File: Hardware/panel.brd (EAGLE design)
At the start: 79 x 43 mm, 18 parts, among them X1 B16B-PHDSS, X2 52746-20

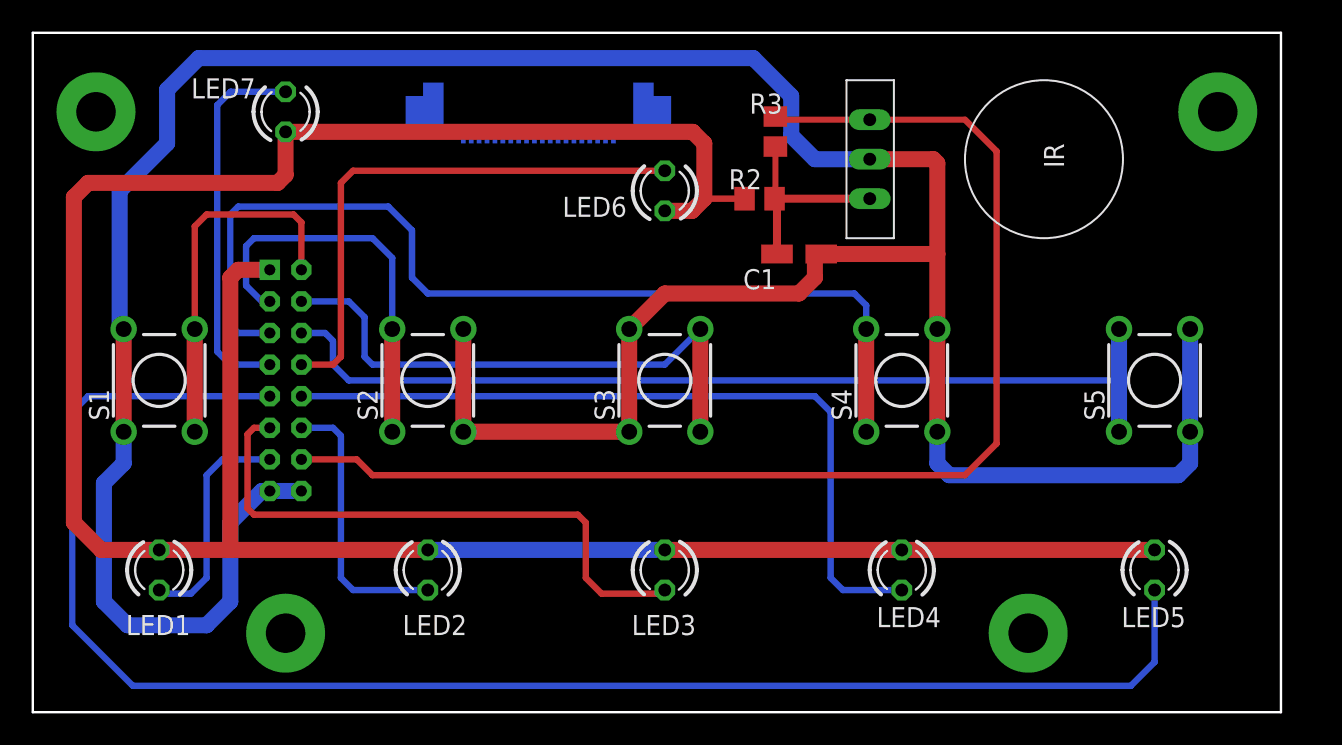
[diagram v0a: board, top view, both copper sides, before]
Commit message: разъем под шлейф,вывод для штатного питания прибора. Сделал цепи комутации кнопок на транзисторе.
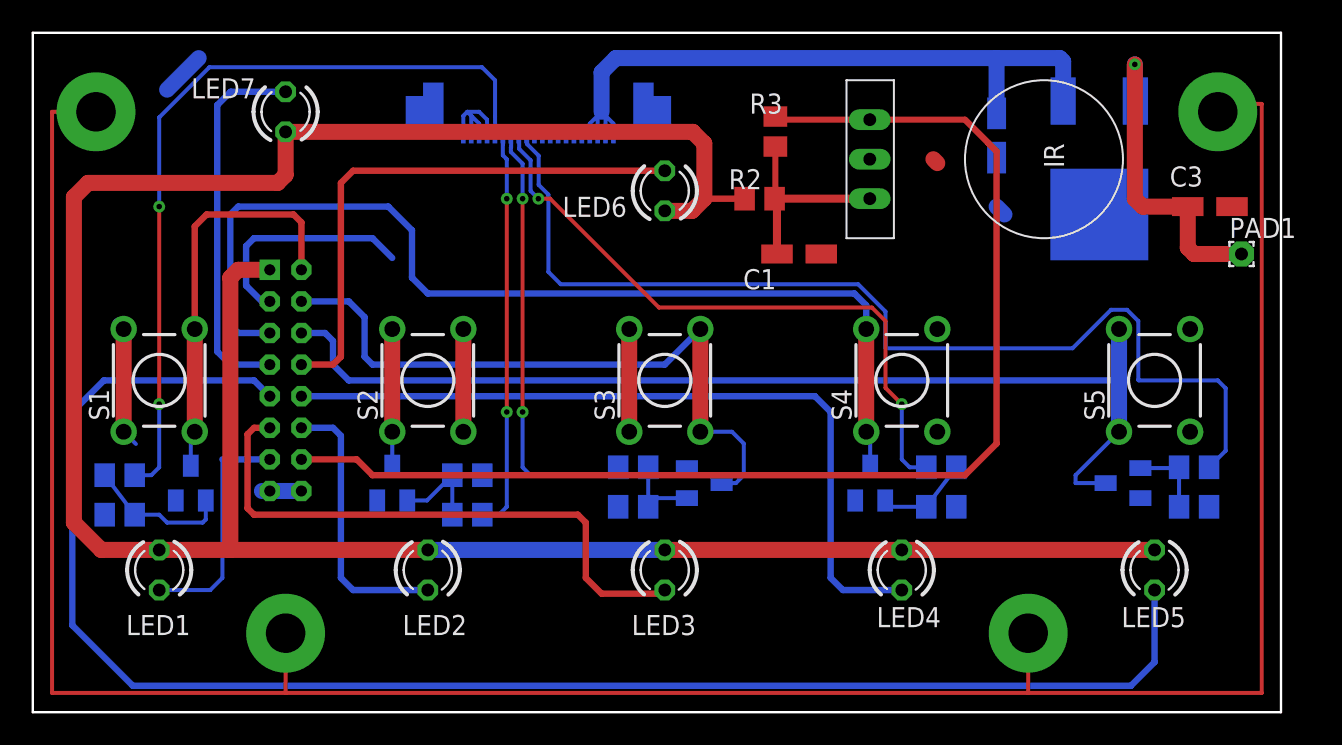
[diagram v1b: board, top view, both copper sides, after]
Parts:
- added C2: 0.33uF, rcl:CT3216
- added C3: 0.1uF, rcl:CT3216
- added PAD1: (no value), wirepad:1,6/0,8
- added Q1, Q2, Q3, Q4, Q5: BC817-40LT1SMD, transistor-npn:SOT23-BEC
- added R1, R10, R11, R12, R4, R5, R6, R7, R8, R9: 4.7k, rcl:R0805
- added U1: MC7805CDT, _hhn_78xx_79xx_NCV78xx_d2pak_dpak:DPAK-3
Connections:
- new net +24V: C2.+, U1.1, X2.17, X2.18, X2.19, X2.20
- new net FF_SIG: R12.2, X2.9
- new net FN_SIG: R10.2, X2.8
- new net LASER_SIG: R8.2, X2.7
- new net N$1: Q1.B, R1.2, R4.1
- new net N$3: S3.1, S3.3
- new net N$4: Q2.B, R5.2, R6.1
- new net N$5: Q3.B, R7.2, R8.1
- new net N$6: Q4.B, R10.1, R9.2
- new net N$7: Q5.B, R11.2, R12.1
- new net PRW_SIG: R4.2, X2.5
- new net SET_SIG: R6.2, X2.6
- new net VOUT_SB: C3.+, PAD1.1, U1.3
- net FFSW: now also Q5.C
- net FNSW: now also Q4.C
- net GND: now also C2.-, C3.-, Q1.E, Q2.E, Q3.E, Q4.E, Q5.E, R1.1, R11.1, R5.1, R7.1, R9.1, U1.4, X2.1, X2.2, X2.3, X2.4; no longer S3.1, S3.3
- net LASERSW: now also Q3.C
- net PWR_SW: now also Q1.C
- net SETSW: now also Q2.C
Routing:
- net FF_SIG: track 0.00 -> 66.0 mm
- net PRW_SIG: track 0.00 -> 50.4 mm, vias 0 -> 2
- net +24V: track 0.00 -> 44.7 mm
- net FN_SIG: track 0.00 -> 40.5 mm, vias 0 -> 2
- net LASER_SIG: track 0.00 -> 27.7 mm, vias 0 -> 2
- net SET_SIG: track 0.00 -> 25.5 mm, vias 0 -> 2
- net VOUT_SB: track 0.00 -> 20.6 mm, vias 0 -> 1
- net N$1: track 0.00 -> 9.13 mm, vias 1 -> 0
- net LASERSW: track 35.8 -> 42.5 mm
- net N$3: track 0.00 -> 6.50 mm, vias 1 -> 0
- net FFSW: track 60.4 -> 66.7 mm
- net N$4: track 0.00 -> 6.01 mm, vias 1 -> 0
- net N$6: track 0.00 -> 5.91 mm
- net N$5: track 0.00 -> 5.18 mm, vias 1 -> 0
- net N$7: track 0.00 -> 4.97 mm
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- added copper zone on layer 1, net GND
- added copper zone on layer 16, net GND

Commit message: переподключил индикаторы через транзисторы. это надо испытать
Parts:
- added Q10, Q11, Q12, Q6, Q7, Q8, Q9: BC807-16LT1SMD, transistor-pnp:SOT23-BEC
- added Q13, Q14, Q15, Q16, Q17, Q18, Q19: BC817-40LT1SMD, transistor-npn:SOT23-BEC
- added R13, R15, R16, R18, R19, R21, R22, R24, R25, R27, R28, R30, R31, R33, R34, R36, R38, R40, R42, R44, R46: 4.7k, rcl:R0805
- added R14, R17, R20, R23, R26, R29, R32: 2.2k, rcl:R0805
- added R35, R37, R39, R41, R43, R45, R47: 800, rcl:R0805
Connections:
- new net ADJLED_SIG: LED2.A, Q9.C, X2.11
- new net DOWNLED_SIG: LED3.A, Q10.C, X2.12
- new net LVLLED_SIG: LED7.A, Q6.C, X2.16
- new net N$10: LED7.K, R14.2
- new net N$11: Q14.B, R36.1, R37.2
- new net N$12: Q7.B, R15.1, R18.1
- new net N$13: LED6.K, R17.2
- new net N$14: Q8.B, R19.1, R21.1
- new net N$15: LED1.K, R20.2
- new net N$16: Q9.B, R22.1, R24.1
- new net N$17: LED2.K, R23.2
- new net N$18: Q10.B, R25.1, R27.1
- new net N$19: LED3.K, R26.2
- new net N$20: Q11.B, R28.1, R30.1
- new net N$21: LED4.K, R29.2
- new net N$22: Q12.B, R31.1, R33.1
- new net N$23: LED5.K, R32.2
- new net N$24: Q13.B, R34.1, R35.2
- new net N$25: Q14.C, R15.2
- new net N$26: Q15.B, R38.1, R39.2
- new net N$27: Q15.C, R31.2
- new net N$28: Q16.B, R40.1, R41.2
- new net N$29: Q16.C, R28.2
- new net N$30: Q17.B, R42.1, R43.2
- new net N$31: Q17.C, R25.2
- new net N$32: Q18.B, R44.1, R45.2
- new net N$33: Q18.C, R22.2
- new net N$34: Q19.B, R46.1, R47.2
- new net N$35: Q19.C, R19.2
- new net N$8: Q6.B, R13.1, R16.1
- new net N$9: Q13.C, R13.2
- new net PWRLED_SIG: LED1.A, Q8.C, X2.10
- new net UPLED_SIG: LED6.A, Q7.C, X2.15
- new net XLED_SIG: LED4.A, Q11.C, X2.13
- new net YLED_SIG: LED5.A, Q12.C, X2.14
- net +24V: now also Q10.E, Q11.E, Q12.E, Q6.E, Q7.E, Q8.E, Q9.E, R16.2, R18.2, R21.2, R24.2, R27.2, R30.2, R33.2
- net +5V: now also R35.1, R37.1, R39.1, R41.1, R43.1, R45.1, R47.1; no longer LED1.A, LED2.A, LED3.A, LED4.A, LED5.A, LED6.A, LED7.A
- net ADJLED: now also Q18.E, R44.2; no longer LED2.K
- net DOWNLED: now also Q17.E, R42.2; no longer LED3.K
- net GND: now also R14.1, R17.1, R20.1, R23.1, R26.1, R29.1, R32.1
- net LVLED: now also Q13.E, R34.2; no longer LED7.K
- net PWRLED: now also Q19.E, R46.2; no longer LED1.K
- net UPLED: now also Q14.E, R36.2; no longer LED6.K
- net XLED: now also Q16.E, R40.2; no longer LED4.K
- net YLED: now also Q15.E, R38.2; no longer LED5.K
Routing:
- net +5V: track 162.0 -> 28.1 mm
- net UPLED: track 34.5 -> 14.8 mm
- net ADJLED: track 17.5 -> 12.8 mm
- net YLED: track 102.5 -> 98.0 mm
- net XLED: track 49.2 -> 45.5 mm
- net LVLED: track 23.9 -> 20.5 mm
- net PWRLED: track 14.8 -> 11.6 mm

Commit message: сделал разводку управляющих и индикаторных цепей на транзисторах. еще не проверял работоспособность решений.
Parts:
- moved R47 237.1 mm to (10.0, 5.50), flipped to the bottom
- moved R46 233.9 mm to (11.0, 2.00), flipped to the bottom, turned to 90 degrees
- moved Q19 227.2 mm to (8.00, 2.50), flipped to the bottom, turned to 180 degrees
- moved R44 222.2 mm to (29.0, 2.50), flipped to the bottom, turned to 90 degrees
- moved R45 221.9 mm to (32.0, 2.50), flipped to the bottom, turned to 270 degrees
- moved R43 218.2 mm to (45.5, 10.5), flipped to the bottom, turned to 270 degrees
- moved Q18 214.3 mm to (25.5, 2.00), flipped to the bottom, turned to 180 degrees
- moved R42 211.2 mm to (44.0, 2.50), flipped to the bottom, turned to 270 degrees
- moved R41 206.9 mm to (63.0, 8.50), flipped to the bottom, turned to 270 degrees
- moved R40 205.6 mm to (58.0, 7.00), flipped to the bottom, turned to 180 degrees
- moved Q17 203.5 mm to (40.0, 2.50), flipped to the bottom, turned to 180 degrees
- moved R36 198.2 mm to (42.5, 31.5), flipped to the bottom
- moved R37 198.0 mm to (47.0, 31.5), flipped to the bottom
- moved R39 196.0 mm to (74.5, 7.00), flipped to the bottom, turned to 180 degrees
- moved R38 195.8 mm to (74.5, 4.50), flipped to the bottom
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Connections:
- removed net N$3: S3.1, S3.3
- net GND: now also S3.1, S3.3
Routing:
- net GND: track 195.1 -> 14.0 mm, vias 4 -> 52
- net +24V: track 44.7 -> 222.9 mm, vias 0 -> 4
- net +5V: track 28.1 -> 179.9 mm, vias 0 -> 10
- net PWRLED_SIG: track 0.00 -> 55.7 mm, vias 0 -> 1
- net YLED_SIG: track 0.00 -> 54.4 mm, vias 0 -> 2
- net XLED_SIG: track 0.00 -> 44.2 mm, vias 0 -> 3
- net ADJLED_SIG: track 0.00 -> 41.4 mm, vias 0 -> 3
- net DOWNLED_SIG: track 0.00 -> 34.7 mm, vias 0 -> 4
- net LVLLED_SIG: track 0.00 -> 31.4 mm
- net UPLED: track 14.8 -> 40.7 mm, vias 0 -> 1
- net XLED: track 45.5 -> 63.7 mm, vias 0 -> 3
- net UPLED_SIG: track 0.00 -> 17.9 mm
- net ADJLED: track 12.8 -> 28.9 mm, vias 0 -> 2
- net DOWNLED: track 36.7 -> 50.7 mm, vias 0 -> 1
- net N$8: track 0.00 -> 13.7 mm
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
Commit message: заменил библиотеку transistor-pnp на пользовательскую, скопировав исходную. Таким образом ушел глюк с исчезновением корпусов транзисторов bc807
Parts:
- Q10, Q11, Q12, Q6, Q7, Q8, Q9: device transistor-pnp:SOT23-BEC -> transistor-pnp_user:SOT23-BEC
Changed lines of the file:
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@@
 </layers>
 <board>
-<fusionsync huburn="a.YnVzaW5lc3M6eWFuZGV4MzMxOA" projecturn="a.YnVzaW5lc3M6eWFuZGV4MzMxOCNEMjAxOTA4MjcyMTA5NzQ0MDY" f3durn="urn:adsk.wipprod:dm.lineage:7har7wxOQ8G1ItqngfwAxw" pcbguid="ca190aa1-6ba8-4648-b4ba-09bebc90098c" lastpulledtime="" lastsyncedchangeguid="" latestrevisionid="1302eb6b-3d8f-46dd-abaf-069875b28583" lastsyncedrevisionid="1302eb6b-3d8f-46dd-abaf-069875b28583" lastboardhashguid="fa5d5c7c-547a-7a33-ed06-7cba926a68bd" lastpushedtime="2020-06-16T15:34:20Z" linktopcb3d="%12"/>
+<fusionsync huburn="a.YnVzaW5lc3M6eWFuZGV4MzMxOA" projecturn="a.YnVzaW5lc3M6eWFuZGV4MzMxOCNEMjAxOTA4MjcyMTA5NzQ0MDY" f3durn="urn:adsk.wipprod:dm.lineage:TgW4m88FTvOA2uf_HjhHag" pcbguid="c6fa01a5-9d4f-491f-97a8-da59074a11a9" lastpulledtime="" lastsyncedchangeguid="" latestrevisionid="998bf07b-379d-46fa-8339-c8b241056cd3" lastsyncedrevisionid="998bf07b-379d-46fa-8339-c8b241056cd3" lastboardhashguid="fa5d5c7c-547a-7a33-ed06-7cba926a68bd" lastpushedtime="2020-06-16T17:29:21Z" linktopcb3d="%12"/>
 <plain>
 <rectangle x1="38.423771875" y1="1.295653125" x2="38.677771875" y2="1.380234375" layer="200" grouprefs="BMP"/>
@@
 <attribute name="VALUE" x="71.865" y="17.04" size="1.27" layer="28" rot="MR180"/>
 </element>
-<element name="Q6" library="transistor-pnp" library_urn="urn:adsk.eagle:library:399" package="SOT23-BEC" package3d_urn="urn:adsk.eagle:package:28748/2" value="BC807-16LT1SMD" x="18.5" y="35" smashed="yes" rot="MR270">
+<element name="Q6" library="transistor-pnp_user" library_urn="urn:adsk.eagle:library:21050097" package="SOT23-BEC" package3d_urn="urn:adsk.eagle:package:28748/2" value="BC807-16LT1SMD" x="18.5" y="35" smashed="yes" rot="MR270">
 <attribute name="NAME" x="18.095" y="33.095" size="1.27" layer="26" rot="MR180"/>
 <attribute name="POPULARITY" value="0" x="10.5" y="42.5" size="1.778" layer="28" rot="MR270" display="off"/>
@@
 <attribute name="VALUE" x="22.54" y="40.135" size="1.27" layer="28" rot="MR270"/>
 </element>
-<element name="Q7" library="transistor-pnp" library_urn="urn:adsk.eagle:library:399" package="SOT23-BEC" package3d_urn="urn:adsk.eagle:package:28748/2" value="BC807-16LT1SMD" x="47.5" y="28.5" smashed="yes" rot="MR270">
+<element name="Q7" library="transistor-pnp_user" library_urn="urn:adsk.eagle:library:21050097" package="SOT23-BEC" package3d_urn="urn:adsk.eagle:package:28748/2" value="BC807-16LT1SMD" x="47.5" y="28.5" smashed="yes" rot="MR270">
 <attribute name="NAME" x="46.675" y="24.415" size="1.27" layer="26" rot="MR180"/>
 <attribute name="POPULARITY" value="0" x="39.5" y="36" size="1.778" layer="28" rot="MR270" display="off"/>
@@
 <attribute name="VALUE" x="45.46" y="34.865" size="1.27" layer="28" rot="MR90"/>
 </element>
-<element name="Q8" library="transistor-pnp" library_urn="urn:adsk.eagle:library:399" package="SOT23-BEC" package3d_urn="urn:adsk.eagle:package:28748/2" value="BC807-16LT1SMD" x="3.5" y="6.5" smashed="yes" rot="MR0">
+<element name="Q8" library="transistor-pnp_user" library_urn="urn:adsk.eagle:library:21050097" package="SOT23-BEC" package3d_urn="urn:adsk.eagle:package:28748/2" value="BC807-16LT1SMD" x="3.5" y="6.5" smashed="yes" rot="MR0">
 <attribute name="NAME" x="1.745" y="6.465" size="1.27" layer="26" rot="MR0"/>
 <attribute name="POPULARITY" value="0" x="11" y="14.5" size="1.778" layer="28" rot="MR0" display="off"/>
@@
 <attribute name="VALUE" x="5.04" y="2.635" size="1.27" layer="28" rot="MR270"/>
 </element>
-<element name="Q9" library="transistor-pnp" library_urn="urn:adsk.eagle:library:399" package="SOT23-BEC" package3d_urn="urn:adsk.eagle:package:28748/2" value="BC807-16LT1SMD" x="20.5" y="6.5" smashed="yes" rot="MR0">
+<element name="Q9" library="transistor-pnp_user" library_urn="urn:adsk.eagle:library:21050097" package="SOT23-BEC" package3d_urn="urn:adsk.eagle:package:28748/2" value="BC807-16LT1SMD" x="20.5" y="6.5" smashed="yes" rot="MR0">
 <attribute name="NAME" x="22.405" y="8.405" size="1.27" layer="26" rot="MR0"/>
 <attribute name="POPULARITY" value="0" x="28" y="14.5" size="1.778" layer="28" rot="MR0" display="off"/>
@@
 <attribute name="VALUE" x="22.04" y="2.635" size="1.27" layer="28" rot="MR270"/>
 </element>
-<element name="Q10" library="transistor-pnp" library_urn="urn:adsk.eagle:library:399" package="SOT23-BEC" package3d_urn="urn:adsk.eagle:package:28748/2" value="BC807-16LT1SMD" x="35" y="6.5" smashed="yes" rot="MR0">
+<element name="Q10" library="transistor-pnp_user" library_urn="urn:adsk.eagle:library:21050097" package="SOT23-BEC" package3d_urn="urn:adsk.eagle:package:28748/2" value="BC807-16LT1SMD" x="35" y="6.5" smashed="yes" rot="MR0">
 <attribute name="NAME" x="34.405" y="7.905" size="1.27" layer="26" rot="MR0"/>
 <attribute name="POPULARITY" value="0" x="50" y="-2" size="1.778" layer="28" rot="MR0" display="off"/>
@@
 <attribute name="VALUE" x="37.04" y="3.135" size="1.27" layer="28" rot="MR270"/>
 </element>
-<element name="Q11" library="transistor-pnp" library_urn="urn:adsk.eagle:library:399" package="SOT23-BEC" package3d_urn="urn:adsk.eagle:package:28748/2" value="BC807-16LT1SMD" x="50.5" y="7" smashed="yes" rot="MR0">
+<element name="Q11" library="transistor-pnp_user" library_urn="urn:adsk.eagle:library:21050097" package="SOT23-BEC" package3d_urn="urn:adsk.eagle:package:28748/2" value="BC807-16LT1SMD" x="50.5" y="7" smashed="yes" rot="MR0">
 <attribute name="NAME" x="48.405" y="5.905" size="1.27" layer="26" rot="MR0"/>
 <attribute name="POPULARITY" value="0" x="73" y="-18" size="1.778" layer="28" rot="MR0" display="off"/>
@@
 <attribute name="VALUE" x="53.04" y="3.135" size="1.27" layer="28" rot="MR270"/>
 </element>
-<element name="Q12" library="transistor-pnp" library_urn="urn:adsk.eagle:library:399" package="SOT23-BEC" package3d_urn="urn:adsk.eagle:package:28748/2" value="BC807-16LT1SMD" x="67" y="6.5" smashed="yes" rot="MR0">
+<element name="Q12" library="transistor-pnp_user" library_urn="urn:adsk.eagle:library:21050097" package="SOT23-BEC" package3d_urn="urn:adsk.eagle:package:28748/2" value="BC807-16LT1SMD" x="67" y="6.5" smashed="yes" rot="MR0">
 <attribute name="NAME" x="67.905" y="8.405" size="1.27" layer="26" rot="MR0"/>
 <attribute name="POPULARITY" value="0" x="74.5" y="14.5" size="1.778" layer="28" rot="MR0" display="off"/>

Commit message: нажал кнопку обновить библиотеки,чтобы компоненты на плате обновились
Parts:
- Q10, Q11, Q12, Q6, Q7, Q8, Q9: device transistor-pnp_user:SOT23-BEC -> transistor-pnp_user:SOT23
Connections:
- net +24V: now also Q10.2, Q11.2, Q12.2, Q6.2, Q7.2, Q8.2, Q9.2; no longer Q10.E, Q11.E, Q12.E, Q6.E, Q7.E, Q8.E, Q9.E
- net ADJLED_SIG: now also Q9.3; no longer Q9.C
- net DOWNLED_SIG: now also Q10.3; no longer Q10.C
- net LVLLED_SIG: now also Q6.3; no longer Q6.C
- net N$12: now also Q7.1; no longer Q7.B
- net N$14: now also Q8.1; no longer Q8.B
- net N$16: now also Q9.1; no longer Q9.B
- net N$18: now also Q10.1; no longer Q10.B
- net N$20: now also Q11.1; no longer Q11.B
- net N$22: now also Q12.1; no longer Q12.B
- net N$8: now also Q6.1; no longer Q6.B
- net PWRLED_SIG: now also Q8.3; no longer Q8.C
- net UPLED_SIG: now also Q7.3; no longer Q7.C
- net XLED_SIG: now also Q11.3; no longer Q11.C
- net YLED_SIG: now also Q12.3; no longer Q12.C
